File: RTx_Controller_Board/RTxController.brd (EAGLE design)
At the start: 161.3 x 90.2 mm, 197 parts, among them IC2 MAX5984C, J22 Debug Header, SW1 COM08720, U1 STM32F407ZXT, U2 TPD4S012, U3 KSZ8081, X4 MINI-USB-32005-301, X8 0826-1X1T-GJ-F

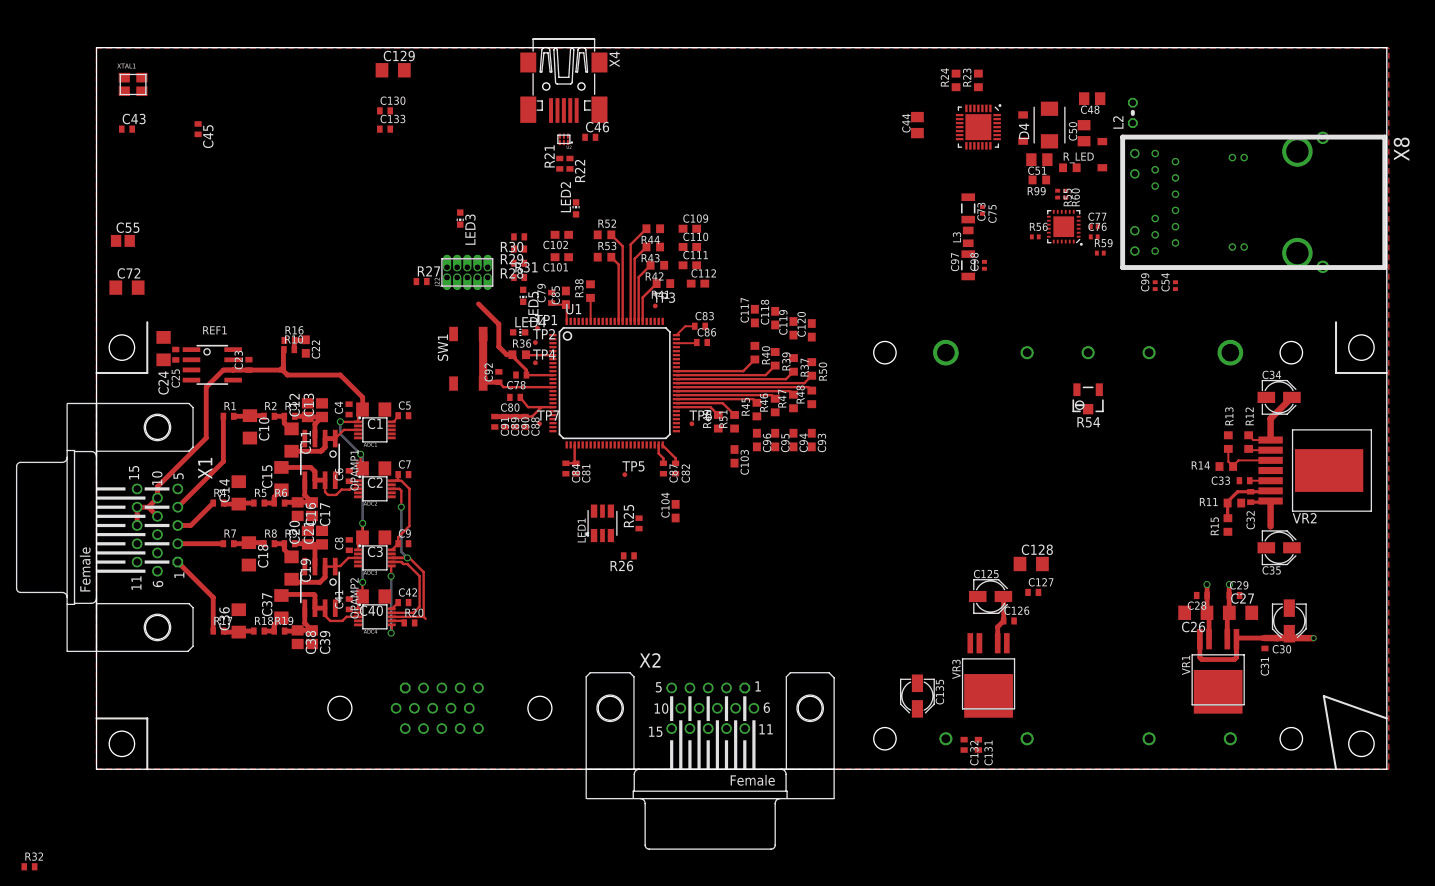
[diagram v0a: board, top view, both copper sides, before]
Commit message: updates made to RTx layout
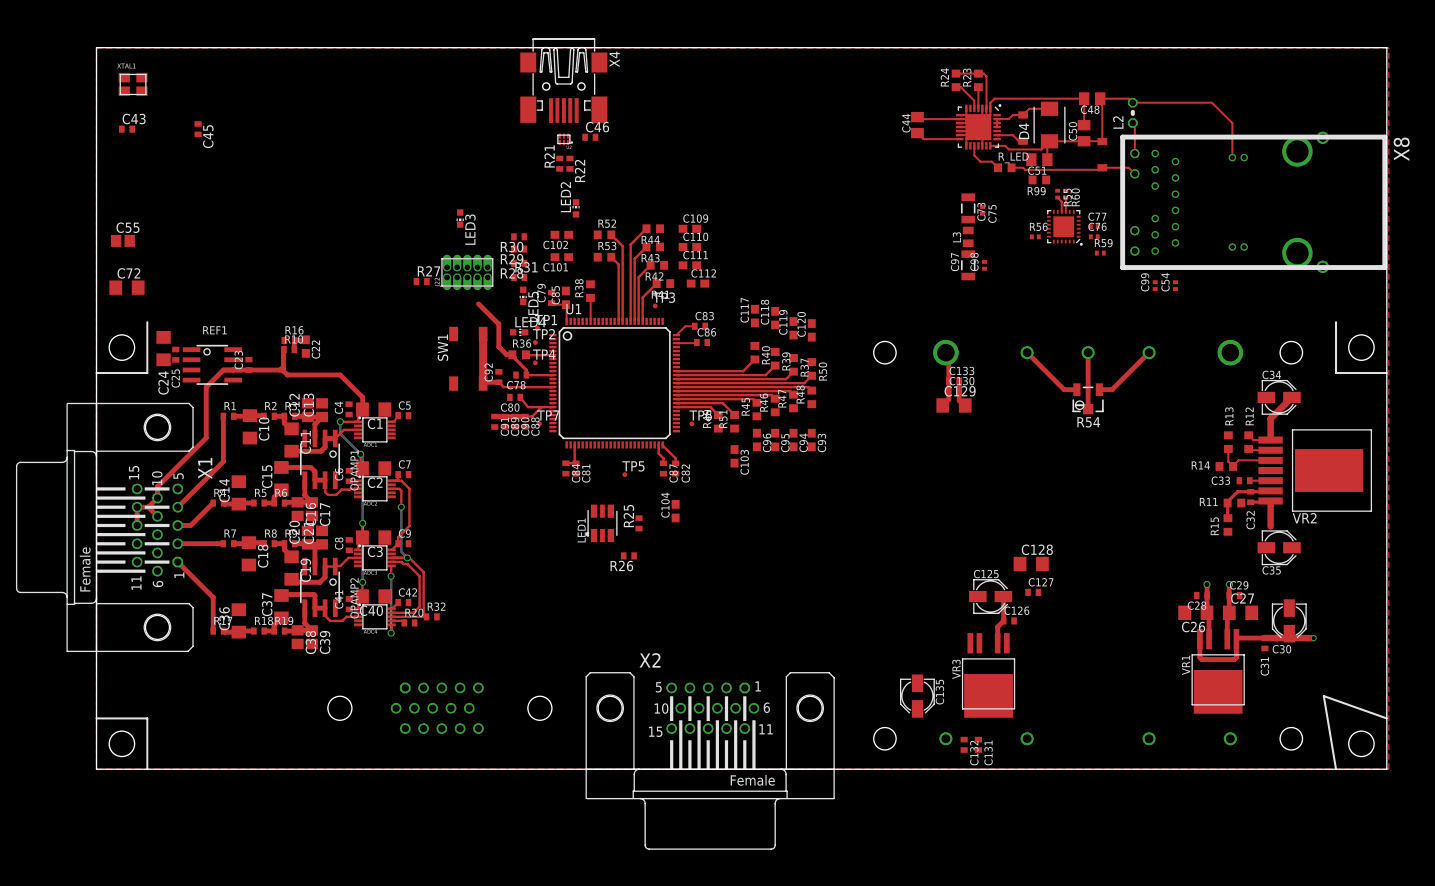
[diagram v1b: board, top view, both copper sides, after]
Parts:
- moved C129 81.7 mm to (107.2, 45.5)
- moved C130 79.3 mm to (107.2, 47.2)
- moved C133 77.8 mm to (107.2, 48.5)
- moved R32 59.2 mm to (41.9, 19.1)
- moved R_LED 8.13 mm to (113.5, 75.2)
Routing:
- net POE-: track 0.00 -> 65.8 mm
- net POE+: track 0.00 -> 51.7 mm
- net POE_LED-: track 0.00 -> 15.9 mm
- net N$67: track 0.00 -> 8.14 mm
- net N$66: track 0.00 -> 8.14 mm
- net PSE_OUTPUT: track 0.00 -> 8.09 mm
- net N$65: track 0.00 -> 7.06 mm
- net N$30: track 0.00 -> 5.59 mm
- net N$29: track 0.00 -> 4.80 mm
- net N$36: track 0.00 -> 3.95 mm
- net POE_LED+: track 0.00 -> 3.92 mm
- net N$34: track 0.00 -> 3.56 mm
- net N$35: track 0.00 -> 2.65 mm
- net ETH_MDIO: track 0.00 -> 1.99 mm
- net N$79: track 0.00 -> 1.78 mm

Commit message: minor updates made
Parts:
- moved R99 0.64 mm to (118.0, 74.3)
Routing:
- net PSE_OUTPUT: track 8.09 -> 38.7 mm
- net N$27: track 0.00 -> 13.0 mm
- net POE_LED-: track 15.9 -> 4.74 mm
- net N$26: track 0.00 -> 9.68 mm
- net VDDA: track 0.00 -> 4.90 mm
- net ACTIVITY_LED: track 0.00 -> 4.23 mm
- net N$15: track 0.00 -> 3.99 mm
- net N$82: track 0.00 -> 3.89 mm
- net POE+: track 51.7 -> 53.6 mm
- net N$80: track 0.00 -> 1.27 mm
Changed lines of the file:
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@@
 <element name="C51" library="motorFeedback" package="C0805K" value="0.1uf 100V" x="117.856" y="76.2" rot="R180"/>
 <element name="D5" library="temp_library" package="SOD-123" value="1N4448" x="115.824" y="81.788" rot="R270"/>
-<element name="R99" library="motorFeedback" package="R0603" value="2.2M" x="117.856" y="73.66" rot="R180"/>
+<element name="R99" library="motorFeedback" package="R0603" value="2.2M" x="117.9576" y="74.295" rot="R180"/>
 <element name="R23" library="motorFeedback" package="R0603" value="1k" x="110.236" y="86.106" rot="R90"/>
 <element name="R24" library="motorFeedback" package="R0603" value="1k" x="107.442" y="86.106" rot="R90"/>
@@
 <wire x1="26.035" y1="41.335" x2="26.416" y2="45.7318" width="0" layer="19" extent="1-1"/>
 <wire x1="26.035" y1="25.333" x2="26.416" y2="29.806" width="0" layer="19" extent="1-1"/>
+<wire x1="121.158" y1="72.312" x2="120.904" y2="67.818" width="0" layer="19" extent="1-1"/>
 <wire x1="57.05" y1="49.76" x2="52.436" y2="49.276" width="0" layer="19" extent="1-1"/>
 </signal>
@@
 <wire x1="141.986" y1="80.772" x2="139.446" y2="83.312" width="0.254" layer="1"/>
 <wire x1="139.446" y1="83.312" x2="129.54" y2="83.312" width="0.254" layer="1"/>
-<wire x1="118.856" y1="76.2" x2="118.706" y2="73.66" width="0" layer="19" extent="1-1"/>
-<wire x1="106.172" y1="52.07" x2="118.706" y2="73.66" width="0" layer="19" extent="1-1"/>
+<wire x1="118.856" y1="76.2" x2="118.856" y2="74.3434" width="0.4064" layer="1"/>
+<wire x1="118.856" y1="74.3434" x2="118.8076" y2="74.295" width="0.4064" layer="1"/>
+<wire x1="106.172" y1="52.07" x2="118.8076" y2="74.295" width="0" layer="19" extent="1-1"/>
 </signal>
 <signal name="ETH_MDC">
@@
 <contactref element="R55" pad="2"/>
 <contactref element="U3" pad="10"/>
-<wire x1="120.654" y1="69.678" x2="120.654" y2="70.94" width="0.254" layer="1"/>
-<wire x1="120.654" y1="70.94" x2="120.142" y2="71.452" width="0.254" layer="1"/>
+<wire x1="120.654" y1="69.678" x2="120.654" y2="70.94" width="0.2286" layer="1"/>
+<wire x1="120.654" y1="70.94" x2="120.142" y2="71.452" width="0.2286" layer="1"/>
 <wire x1="57.05" y1="42.26" x2="120.654" y2="69.678" width="0" layer="19" extent="1-1"/>
 </signal>
@@
 <contactref element="C54" pad="2"/>
 <contactref element="X8" pad="6"/>
-<wire x1="134.874" y1="60.882" x2="134.874" y2="65.786" width="0" layer="19" extent="1-1"/>
+<wire x1="134.874" y1="60.882" x2="134.874" y2="65.786" width="0.4064" layer="1"/>
 </signal>
 <signal name="ETH_RMII_REF_CLK">
@@
 <contactref element="U3" pad="9"/>
 <contactref element="R60" pad="2"/>
-<wire x1="121.154" y1="69.678" x2="121.154" y2="71.448" width="0.254" layer="1"/>
 <wire x1="121.154" y1="71.448" x2="121.158" y2="71.452" width="0.254" layer="1"/>
+<wire x1="121.154" y1="69.678" x2="121.154" y2="71.448" width="0.2286" layer="1"/>
 </signal>
 <signal name="N$80">
@@
 <contactref element="U3" pad="1"/>
 <contactref element="C76" pad="1"/>
-<wire x1="124.284" y1="66.548" x2="124.284" y2="67.818" width="0" layer="19" extent="1-1"/>
-<wire x1="122.764" y1="66.568" x2="124.284" y2="66.548" width="0" layer="19" extent="1-1"/>
+<wire x1="124.284" y1="66.548" x2="124.284" y2="67.818" width="0.4064" layer="1"/>
+<wire x1="124.284" y1="66.548" x2="122.764" y2="66.568" width="0" layer="19" extent="1-1"/>
 </signal>
 <signal name="ACTIVITY_LED">
 <contactref element="U3" pad="23"/>
 <contactref element="R59" pad="1"/>
-<wire x1="121.654" y1="65.958" x2="125.046" y2="64.516" width="0" layer="19" extent="1-1"/>
+<wire x1="125.046" y1="64.516" x2="122.682" y2="64.516" width="0.254" layer="1"/>
+<wire x1="122.682" y1="64.516" x2="121.666" y2="65.532" width="0.254" layer="1"/>
+<wire x1="121.666" y1="65.532" x2="121.666" y2="65.946" width="0.254" layer="1"/>
+<wire x1="121.666" y1="65.946" x2="121.654" y2="65.958" width="0.254" layer="1"/>
 </signal>
 <signal name="N$82">
 <contactref element="C99" pad="2"/>
 <contactref element="X8" pad="12"/>
-<wire x1="132.334" y1="60.882" x2="132.334" y2="64.77" width="0" layer="19" extent="1-1"/>
+<wire x1="132.334" y1="64.77" x2="132.334" y2="60.882" width="0.4064" layer="1"/>
 </signal>
 <signal name="N$21">
@@
 <contactref element="U3" pad="5"/>
 <contactref element="X8" pad="10"/>
-<wire x1="122.764" y1="68.568" x2="132.334" y2="68.834" width="0" layer="19" extent="1-1"/>
+<wire x1="122.764" y1="68.568" x2="132.068" y2="68.568" width="0.2286" layer="1"/>
+<wire x1="132.068" y1="68.568" x2="132.334" y2="68.834" width="0.2286" layer="1"/>
 </signal>
 <signal name="N$27">
 <contactref element="U3" pad="4"/>
 <contactref element="X8" pad="4"/>
-<wire x1="122.764" y1="68.068" x2="134.874" y2="69.85" width="0" layer="19" extent="1-1"/>
+<wire x1="122.764" y1="68.068" x2="129.028" y2="68.068" width="0.2286" layer="1"/>
+<wire x1="129.028" y1="68.068" x2="129.032" y2="68.072" width="0.2286" layer="1"/>
+<wire x1="129.032" y1="68.072" x2="129.0574" y2="68.072" width="0.2286" layer="1"/>
+<wire x1="129.0574" y1="68.072" x2="129.2098" y2="68.2244" width="0.2286" layer="1"/>
+<wire x1="129.2098" y1="68.2244" x2="131.6736" y2="68.2244" width="0.2286" layer="1"/>
+<wire x1="131.6736" y1="68.2244" x2="131.826" y2="68.072" width="0.2286" layer="1"/>
+<wire x1="131.826" y1="68.072" x2="133.096" y2="68.072" width="0.2286" layer="1"/>
+<wire x1="133.096" y1="68.072" x2="134.874" y2="69.85" width="0.2286" layer="1"/>
 </signal>
 <signal name="N$28">
@@
 <contactref element="D3" pad="P$1"/>
 <contactref element="X8" pad="18"/>
-<wire x1="114.388" y1="75.184" x2="115.824" y2="75.184" width="0.254" layer="1"/>
-<wire x1="115.824" y1="75.184" x2="116.078" y2="74.93" width="0.254" layer="1"/>
-<wire x1="116.078" y1="74.93" x2="125.476" y2="74.93" width="0.254" layer="1"/>
 <wire x1="125.476" y1="74.93" x2="125.73" y2="75.184" width="0.254" layer="1"/>
 <wire x1="125.73" y1="75.184" x2="129.032" y2="75.184" width="0.254" layer="1"/>
 <wire x1="129.032" y1="75.184" x2="129.794" y2="74.422" width="0.254" layer="1"/>
+<wire x1="114.388" y1="75.184" x2="125.476" y2="74.93" width="0" layer="19" extent="1-1"/>
 </signal>
 <signal name="PSE_OUTPUT">
@@
 <wire x1="119.126" y1="82.558" x2="116.594" y2="82.558" width="0.254" layer="1"/>
 <wire x1="116.594" y1="82.558" x2="115.824" y2="81.788" width="0.254" layer="1"/>
-<wire x1="117.006" y1="73.66" x2="141.986" y2="65.278" width="0" layer="19" extent="1-1"/>
-<wire x1="116.856" y1="76.2" x2="117.006" y2="73.66" width="0" layer="19" extent="1-1"/>
-<wire x1="115.824" y1="81.788" x2="116.856" y2="76.2" width="0" layer="19" extent="1-1"/>
+<wire x1="116.856" y1="76.2" x2="116.856" y2="74.5466" width="0.4064" layer="1"/>
+<wire x1="116.856" y1="74.5466" x2="117.1076" y2="74.295" width="0.4064" layer="1"/>
+<wire x1="141.986" y1="65.278" x2="141.478" y2="65.278" width="0.4064" layer="1"/>
+<wire x1="141.478" y1="65.278" x2="135.89" y2="70.866" width="0.4064" layer="1"/>
+<wire x1="135.89" y1="70.866" x2="125.73" y2="70.866" width="0.4064" layer="1"/>
+<wire x1="125.73" y1="70.866" x2="123.444" y2="73.152" width="0.4064" layer="1"/>
+<wire x1="123.444" y1="73.152" x2="118.2506" y2="73.152" width="0.4064" layer="1"/>
+<wire x1="118.2506" y1="73.152" x2="117.1076" y2="74.295" width="0.4064" layer="1"/>
+<wire x1="116.856" y1="76.2" x2="115.824" y2="81.788" width="0" layer="19" extent="1-1"/>
 </signal>
 <signal name="N$34">
@@
 <contactref element="X8" pad="20"/>
 <contactref element="R59" pad="2"/>
-<wire x1="125.906" y1="64.516" x2="129.794" y2="64.77" width="0" layer="19" extent="1-1"/>
+<wire x1="125.906" y1="64.516" x2="129.54" y2="64.516" width="0.4064" layer="1"/>
+<wire x1="129.54" y1="64.516" x2="129.794" y2="64.77" width="0.4064" layer="1"/>
 </signal>
 <signal name="N$25">
